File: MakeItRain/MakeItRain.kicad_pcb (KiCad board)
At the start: 4 copper layers, 151.1 x 71.1 mm, 83 parts, among them IC2 LM2597MX-5.0_NOPB, IC3 OPA2340PA, IC4 LTV-846S, J1 Conn_02x15_Odd_Even, J2 Conn_02x19_Odd_Even, J3 Conn_01x19, J4 Conn_01x01, P1 Screw_Terminal_01x02, Q1 2N7000, Q10 2N7000, Q11 2N7000, Q12 IRF9Z34NPBF, Q13 IRF9Z34NPBF, Q2 2N7000, Q3 IRF9Z34NPBF, Q4 2N7000, Q5 2N7000, Q6 IRF9Z34NPBF, Q7 2N7000, Q8 2N7000, Q9 IRF9Z34NPBF, U2 178.6165.0001

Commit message: preautoroute
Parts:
- moved C6 6.14 mm to (52.2, 100.1), turned to 0 degrees
- moved C7 2.73 mm to (59.8, 88.9)
- moved IC2 2.65 mm to (55.0, 94.4)
- moved R22 0.95 mm to (49.0, 93.4)
- moved R21 0.68 mm to (167.4, 105.2)
- moved Q13 0.68 mm to (174.3, 105.2)
- moved U2 0.68 mm to (165.0, 112.3)
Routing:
- net +5V: track 0.00 -> 156.2 mm
- net +3V3: track 0.00 -> 126.8 mm
- net GND: track 0.00 -> 88.1 mm
- net +VDC: track 0.00 -> 59.7 mm
- net /Zone3IO/ZoneOutput: track 0.00 -> 31.6 mm
- net /Zone2IO/ZoneOutput: track 0.00 -> 30.9 mm
- net /Zone4IO/ZoneOutput: track 0.00 -> 30.9 mm
- net /Zone1IO/ZoneOutput: track 0.00 -> 29.6 mm
- net Net-(Q12-Pad1): track 0.00 -> 17.9 mm
- net Net-(Q9-Pad1): track 0.00 -> 14.8 mm
- net Net-(Q6-Pad1): track 0.00 -> 14.6 mm
- net Net-(Q3-Pad1): track 0.00 -> 13.3 mm
- net Net-(D10-Pad1): track 0.00 -> 12.4 mm
- net Net-(P1-Pad1): track 0.00 -> 9.22 mm
- net Net-(Q13-Pad1): track 0.00 -> 7.95 mm
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- added copper zone on F.Cu, net +VDC
- added copper zone on B.Cu, net Net-(Q13-Pad3)

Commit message: Routed. DRC'ed. and Fab Files have been updated.
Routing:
- net GND: track 88.1 -> 294.7 mm, vias 0 -> 4
- net D23: track 0.00 -> 110.3 mm
- net Net-(IC3-Pad5): track 0.00 -> 109.0 mm, vias 0 -> 2
- net /Zone4IO/ZoneInput: track 0.00 -> 102.3 mm
- net D39: track 0.00 -> 102.3 mm
- net D19: track 0.00 -> 98.0 mm, vias 0 -> 2
- net D22: track 0.00 -> 92.9 mm
- net D2: track 0.00 -> 90.5 mm
- net D5: track 0.00 -> 89.2 mm, vias 0 -> 1
- net D18: track 0.00 -> 85.7 mm
- net /Zone3IO/ZoneInput: track 0.00 -> 84.6 mm
- net D21: track 0.00 -> 82.6 mm, vias 0 -> 1
- net D35: track 0.00 -> 81.6 mm
- net D32: track 0.00 -> 77.9 mm, vias 0 -> 1
- net TX: track 0.00 -> 76.7 mm
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
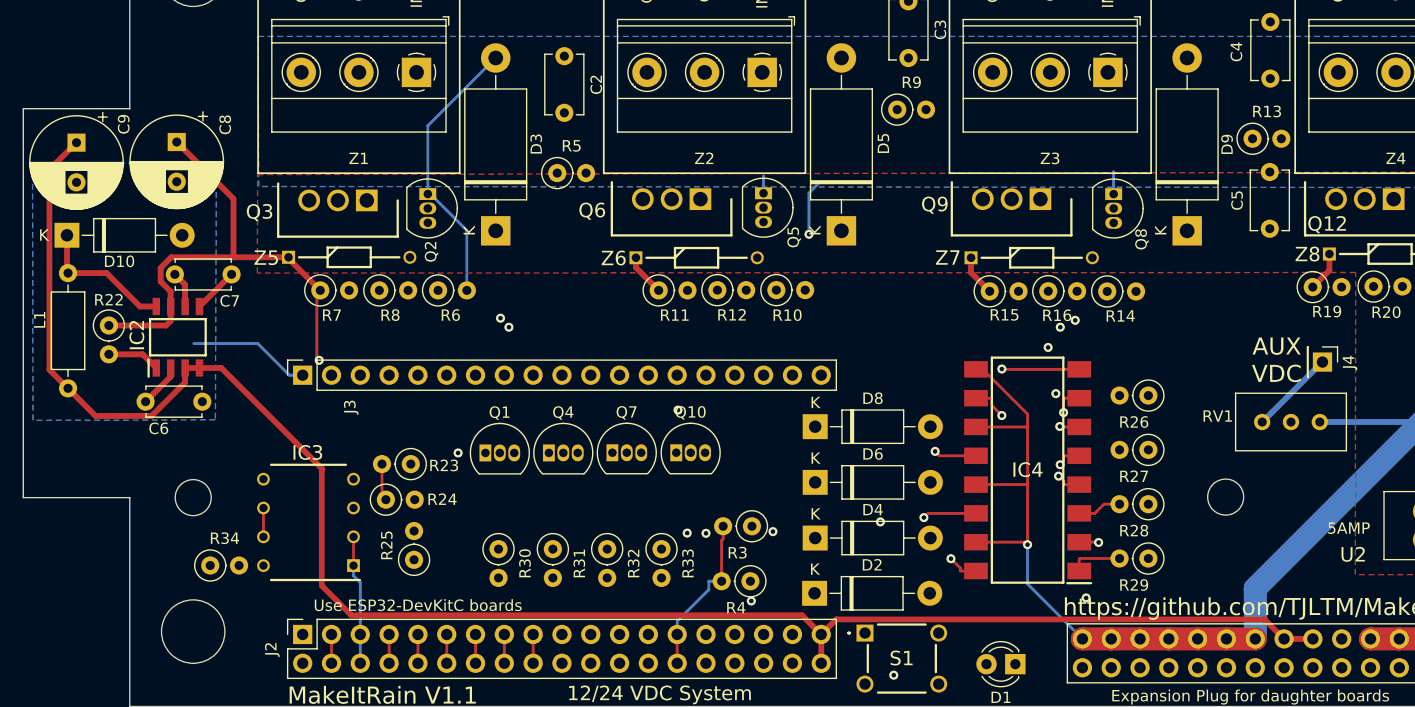
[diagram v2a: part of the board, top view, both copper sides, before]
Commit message: due to lack of chips (LM2597) i'm switching (no pun intended) to having the power system be a daughter board that can be plugged in once i find some replacements.
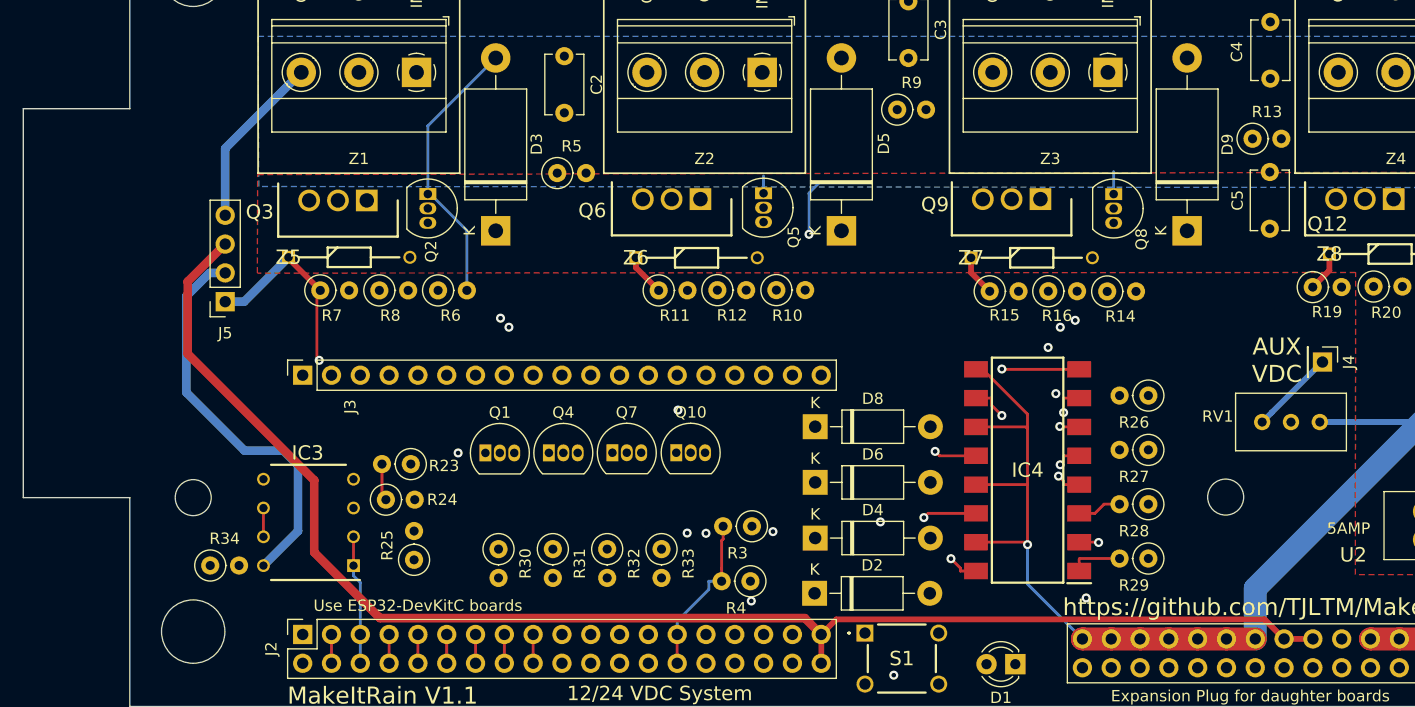
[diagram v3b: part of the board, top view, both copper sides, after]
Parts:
- removed C6, C7: 0.1uF, Capacitor_THT:C_Disc_D4.7mm_W2.5mm_P5.00mm
- removed C8: 68uF, Capacitor_THT:CP_Radial_D8.0mm_P3.50mm
- removed C9: 120uF, Capacitor_THT:CP_Radial_D8.0mm_P3.50mm
- removed D10: 1N5817, Diode_THT:D_DO-41_SOD81_P10.16mm_Horizontal
- removed IC2: LM2597MX-5.0_NOPB, SamacSys_Parts:SOIC127P600X175-8N
- removed L1: 150uH, Inductor_THT:L_Axial_L6.6mm_D2.7mm_P10.16mm_Horizontal_Vishay_IM-2
- removed R22: 10k, Resistor_THT:R_Axial_DIN0207_L6.3mm_D2.5mm_P2.54mm_Vertical
- added J5: Conn_01x04, Connector_PinSocket_2.54mm:PinSocket_1x04_P2.54mm_Vertical, F.Cu at (59.2, 91.3)
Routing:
- net +3V3: track 127.8 -> 163.2 mm
- net +5V: track 156.2 -> 128.0 mm
- net +VDC: track 85.9 -> 58.6 mm
- net Net-(D10-Pad1): track 12.4 -> 0.00 mm
- net Net-(C6-Pad1): track 4.93 -> 0.00 mm
- net Net-(IC2-Pad1): track 4.68 -> 0.00 mm
- net Net-(C7-Pad1): track 4.00 -> 0.00 mm
- net GND: track 294.7 -> 296.1 mm

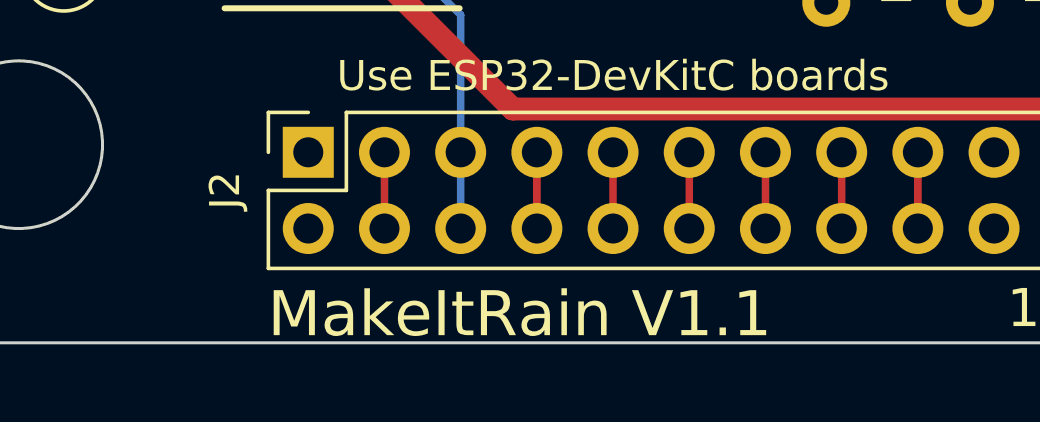
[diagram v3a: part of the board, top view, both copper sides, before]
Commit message: bumped Version on silkscreen to 1.2. Still need to place some mounting holes if needed for the power daughter board.
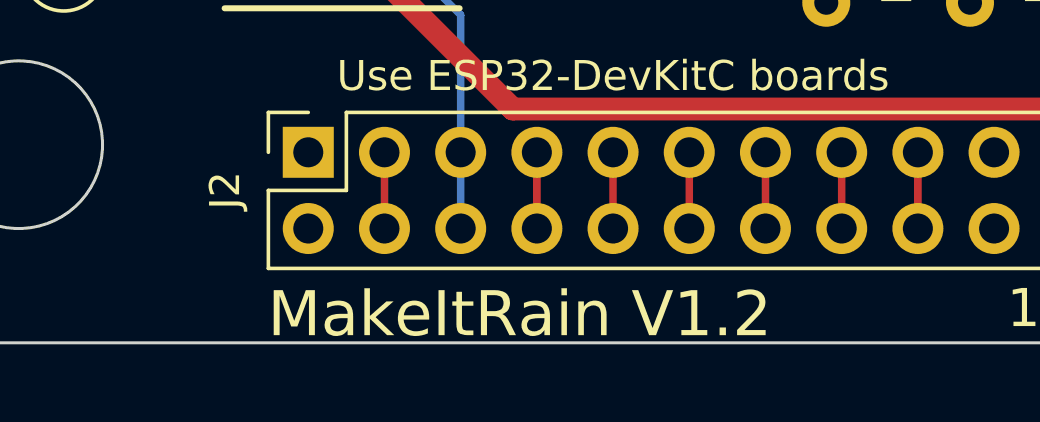
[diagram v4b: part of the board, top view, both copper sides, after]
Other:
- board text added: "MakeItRain V1.2"
- board text removed: "MakeItRain V1.1"
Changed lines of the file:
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@@
     (effects (font (size 1.5 1.905) (thickness 0.3)))
   )
-  (gr_text "MakeItRain V1.1" (at 73.089135 126.050282) (layer "F.SilkS")
+  (gr_text "MakeItRain V1.2" (at 73.089135 126.050282) (layer "F.SilkS")
     (effects (font (size 1.5 1.5) (thickness 0.3)))
   )

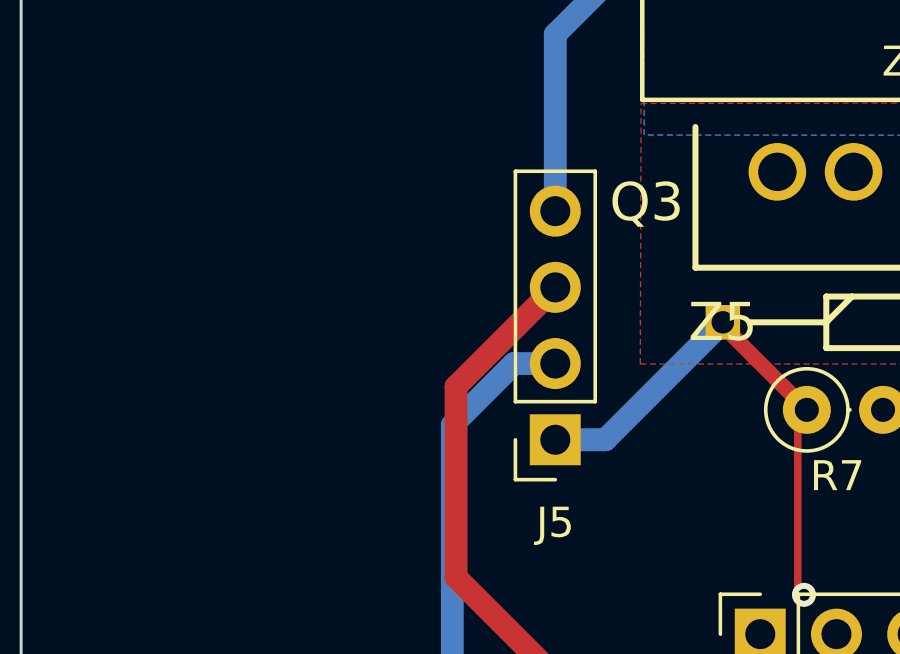
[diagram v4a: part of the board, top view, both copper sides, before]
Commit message: updated Silkscreen to have the power header values. updated Fab Files.
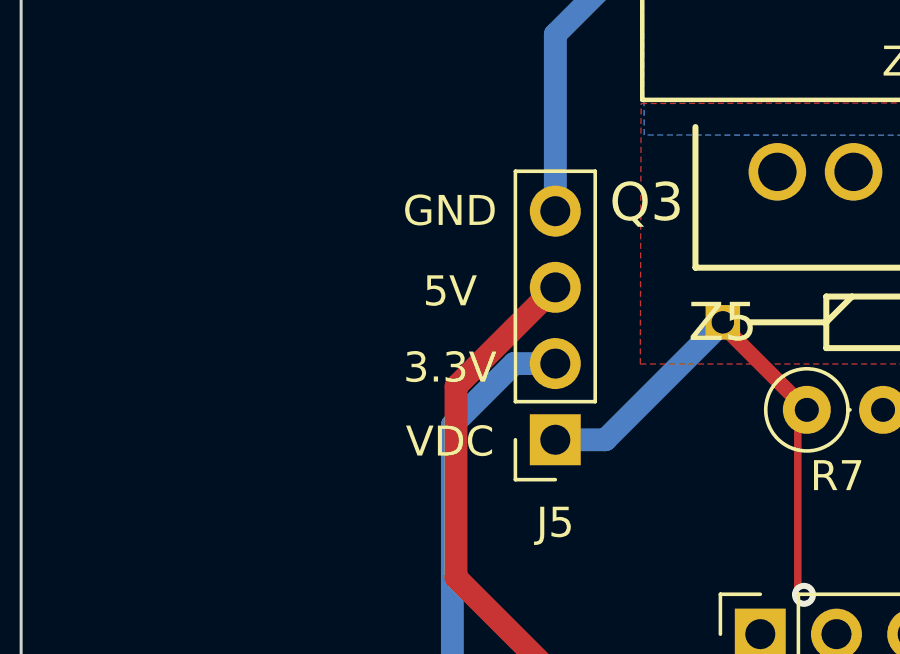
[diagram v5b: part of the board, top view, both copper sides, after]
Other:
- board text added: "3.3V"
- board text added: "5V"
- board text added: "VDC"
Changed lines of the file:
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@@
+    (effects (font (size 1 1) (thickness 0.15)))
+  )
+  (gr_text "3.3V" (at 55.697284 88.906695) (layer "F.SilkS")
     (effects (font (size 1 1) (thickness 0.15)))
   )
   (gr_text "AUX\nVDC" (at 151.937112 96.47999) (layer "F.SilkS")
     (effects (font (size 1.5 1.5) (thickness 0.3)))
+  )
+  (gr_text "5V" (at 55.697284 86.365881) (layer "F.SilkS")
+    (effects (font (size 1 1) (thickness 0.15)))
   )
   (gr_text "ZONE 1" (at 71.00703 59.581504) (layer "F.SilkS")
@@
     (effects (font (size 1 1) (thickness 0.15)))
   )
+  (gr_text "GND" (at 55.697284 83.68651) (layer "F.SilkS")
+    (effects (font (size 1 1) (thickness 0.15)))
+  )
   (gr_text "GND" (at 65.92703 63.391504 90) (layer "F.SilkS")
     (effects (font (size 1 1) (thickness 0.15)))
   )
+  (gr_text "VDC" (at 55.697284 91.374391) (layer "F.SilkS")
+    (effects (font (size 1 1) (thickness 0.15)))
+  )

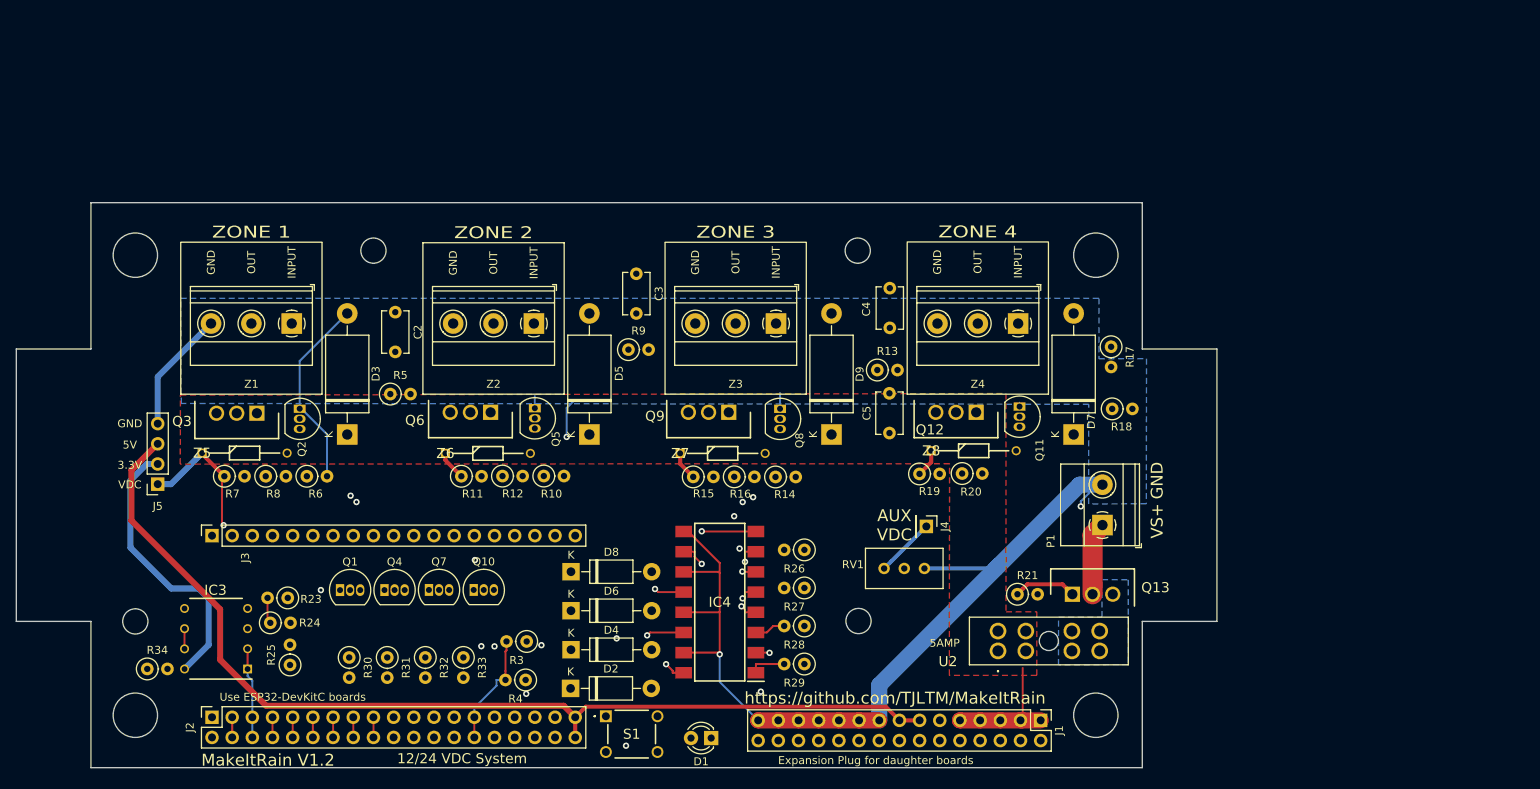
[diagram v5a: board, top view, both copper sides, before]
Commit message: cleaned up PCB of traces that have been deleted in the schematic.
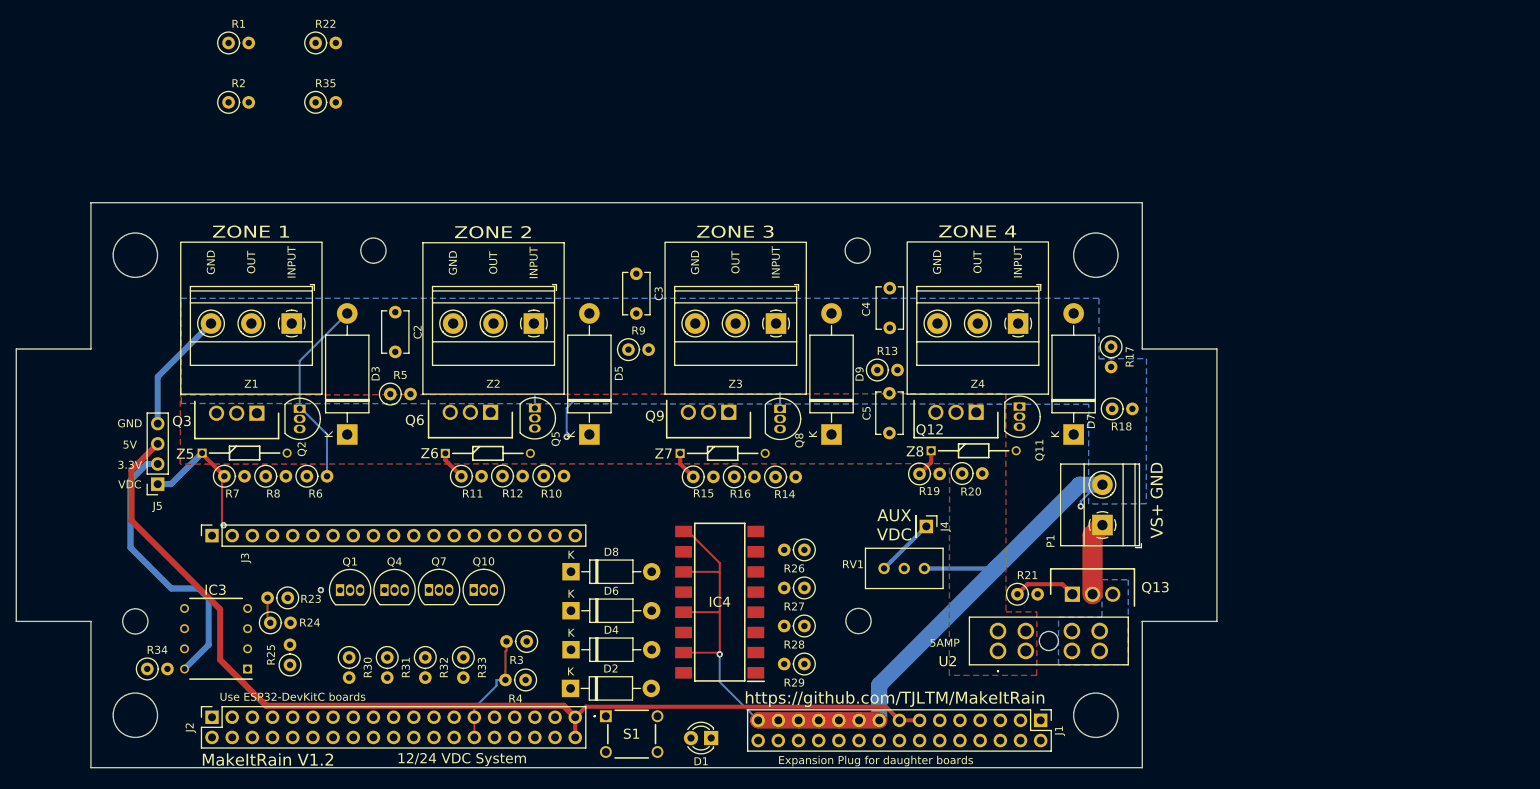
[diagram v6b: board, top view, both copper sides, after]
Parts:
- added R1: 470, Resistor_THT:R_Axial_DIN0207_L6.3mm_D2.5mm_P2.54mm_Vertical, F.Cu at (68.1, 35.8)
- added R2: 470, Resistor_THT:R_Axial_DIN0207_L6.3mm_D2.5mm_P2.54mm_Vertical, F.Cu at (68.1, 43.3)
- added R22: 470, Resistor_THT:R_Axial_DIN0207_L6.3mm_D2.5mm_P2.54mm_Vertical, F.Cu at (79.1, 35.8)
- added R35: 470, Resistor_THT:R_Axial_DIN0207_L6.3mm_D2.5mm_P2.54mm_Vertical, F.Cu at (79.1, 43.3)
- R13, R17, R5, R9: value 1M -> 5k
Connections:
- D1 pad 2: D21 -> D27
- D2 pad 1: Net-(D2-Pad1) -> /Zone1IO/ZoneInput
- D2 pad 2: /InputIsolation/1in -> Net-(Q1-Pad2)
- D4 pad 1: Net-(D4-Pad1) -> /Zone2IO/ZoneInput
- D4 pad 2: /InputIsolation/2in -> Net-(Q4-Pad2)
- D6 pad 1: Net-(D6-Pad1) -> /Zone3IO/ZoneInput
- D6 pad 2: /InputIsolation/3in -> Net-(Q7-Pad2)
- D8 pad 1: Net-(D8-Pad1) -> /Zone4IO/ZoneInput
- D8 pad 2: /InputIsolation/4in -> Net-(Q10-Pad2)
- IC3 pad 6: D34 -> D32
- IC3 pad 7: D34 -> D32
- IC4 pad 10: D12 -> D39
- IC4 pad 12: D14 -> D36
- IC4 pad 14: D27 -> D35
- IC4 pad 16: D26 -> D34
- J1 pad 10: D18 -> unconnected-(J1-Pad10)
- J1 pad 12: D5 -> unconnected-(J1-Pad12)
- J1 pad 14: D35 -> unconnected-(J1-Pad14)
- J1 pad 16: D32 -> unconnected-(J1-Pad16)
- J1 pad 18: D33 -> unconnected-(J1-Pad18)
- J1 pad 2: D39 -> D22
- J1 pad 20: D25 -> unconnected-(J1-Pad20)
- J1 pad 22: D21 -> unconnected-(J1-Pad22)
- J1 pad 24: D4 -> unconnected-(J1-Pad24)
- J1 pad 26: D0 -> unconnected-(J1-Pad26)
- J1 pad 4: AuxVoltage -> D21
- J1 pad 6: D23 -> unconnected-(J1-Pad6)
- J1 pad 8: D19 -> unconnected-(J1-Pad8)
- Q1 pad 2: /Zone1IO/ZoneInput -> Net-(Q1-Pad2)
- Q1 pad 3: Net-(D2-Pad1) -> /InputIsolation/1in
- Q10 pad 2: /Zone4IO/ZoneInput -> Net-(Q10-Pad2)
- Q10 pad 3: Net-(D8-Pad1) -> /InputIsolation/4in
- Q11 pad 2: D2 -> /Zone4IO/ZoneOutputTTL
- Q2 pad 2: D17 -> /Zone1IO/ZoneOutputTTL
- Q4 pad 2: /Zone2IO/ZoneInput -> Net-(Q4-Pad2)
- Q4 pad 3: Net-(D4-Pad1) -> /InputIsolation/2in
- Q5 pad 2: D16 -> /Zone2IO/ZoneOutputTTL
- Q7 pad 2: /Zone3IO/ZoneInput -> Net-(Q7-Pad2)
- Q7 pad 3: Net-(D6-Pad1) -> /InputIsolation/3in
- Q8 pad 2: D15 -> /Zone3IO/ZoneOutputTTL
- R10 pad 1: D16 -> /Zone2IO/ZoneOutputTTL
- R13 pad 1: /Zone3IO/ZoneInput -> Net-(Q7-Pad2)
- R14 pad 1: D15 -> /Zone3IO/ZoneOutputTTL
- R17 pad 1: /Zone4IO/ZoneInput -> Net-(Q10-Pad2)
- R18 pad 1: D2 -> /Zone4IO/ZoneOutputTTL
- R3 pad 1: D22 -> D33
- R30 pad 2: D26 -> D34
- R31 pad 2: D27 -> D35
- R32 pad 2: D14 -> D36
- R33 pad 2: D12 -> D39
- R34 pad 1: D34 -> D32
- R5 pad 1: /Zone1IO/ZoneInput -> Net-(Q1-Pad2)
- R6 pad 1: D17 -> /Zone1IO/ZoneOutputTTL
- R9 pad 1: /Zone2IO/ZoneInput -> Net-(Q4-Pad2)
- S1 pad 4: D22 -> D33
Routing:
- net D23: track 110.3 -> 0.00 mm
- net Net-(IC3-Pad5): track 109.0 -> 0.00 mm, vias 2 -> 0
- net /Zone4IO/ZoneInput: track 102.3 -> 0.00 mm
- net D39: track 102.3 -> 0.00 mm
- net D19: track 98.0 -> 0.00 mm, vias 2 -> 0
- net D22: track 92.9 -> 0.00 mm
- net D2: track 90.5 -> 0.00 mm
- net D5: track 89.2 -> 0.00 mm, vias 1 -> 0
- net D18: track 85.7 -> 0.00 mm
- net /Zone3IO/ZoneInput: track 84.6 -> 0.00 mm
- net D21: track 82.6 -> 0.00 mm, vias 1 -> 0
- net D35: track 81.6 -> 0.00 mm
- net D32: track 77.9 -> 0.00 mm, vias 1 -> 0
- net TX: track 76.7 -> 0.00 mm
- net D33: track 71.8 -> 0.00 mm
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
